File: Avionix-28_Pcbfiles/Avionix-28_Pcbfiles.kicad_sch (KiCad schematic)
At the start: 13 parts, among them J1 Conn_01x02_Pin, J2 Conn_01x02_Pin, U1 TPS54202DDCR

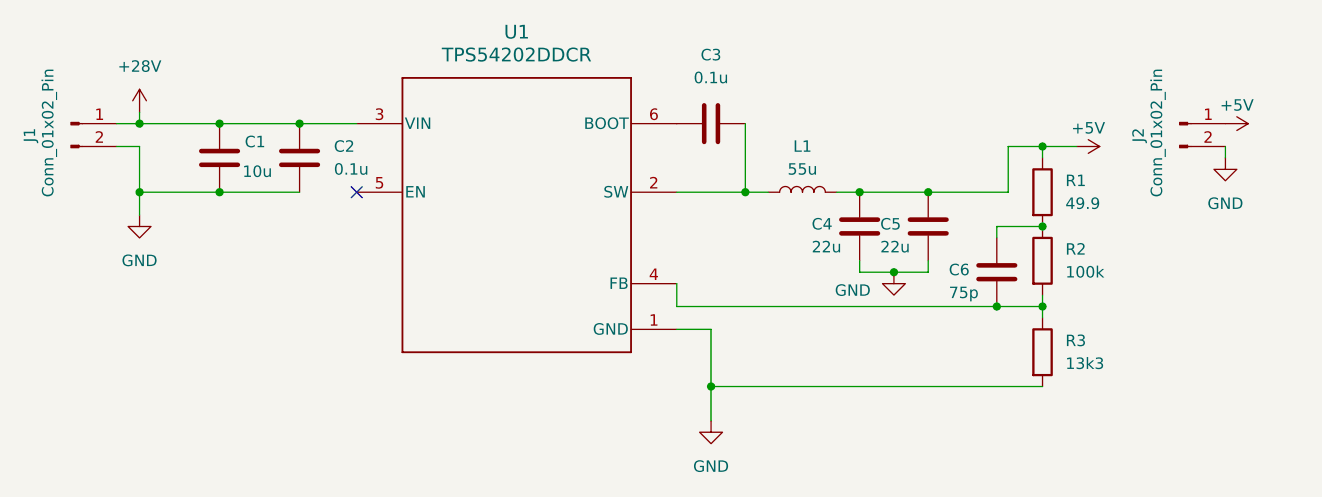
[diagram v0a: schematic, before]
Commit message: changed inductor value and assigned footprints
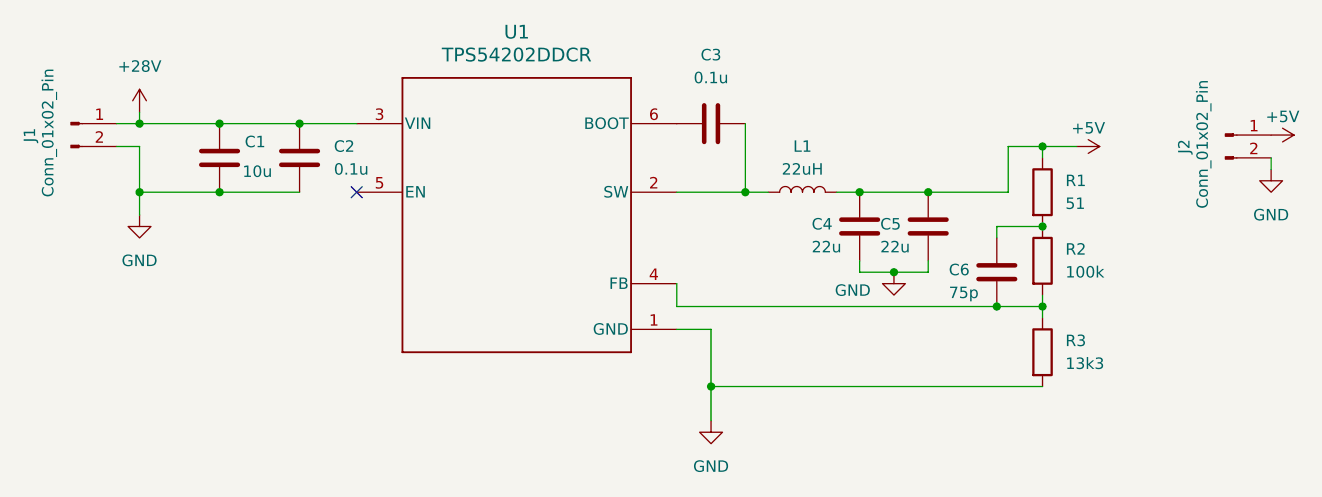
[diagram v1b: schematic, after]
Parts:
- C1, C4, C5: footprint (none) -> Capacitor_SMD:C_1210_3225Metric
- C2, C3: footprint (none) -> Capacitor_SMD:C_0402_1005Metric
- C6: footprint (none) -> Capacitor_SMD:C_0805_2012Metric
- J1, J2: footprint Avionix_fprints:CUI_TB007-508-02BE -> Screw_terminal:Connector_PinHeader_3.81
- L1: value 55u -> 22uH
- R1: value 49.9 -> 51; footprint (none) -> Resistor_SMD:R_0805_2012Metric
- R2, R3: footprint (none) -> Resistor_SMD:R_0805_2012Metric
- U1: footprint DDC0006A_N -> Screw_terminal:DDC0006A_N
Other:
- moved on the sheet: J2
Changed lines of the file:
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@@
 	(wire
 		(pts
-			(xy 172.72 77.47) (xy 172.72 76.2)
+			(xy 177.8 78.74) (xy 177.8 77.47)
 		)
 		(stroke
@@
 			)
 		)
-		(property "Footprint" ""
+		(property "Footprint" "Resistor_SMD:R_0805_2012Metric"
 			(at 150.622 99.06 90)
 			(hide yes)
@@
 	(symbol
 		(lib_id "power:GND")
-		(at 172.72 77.47 0)
+		(at 177.8 78.74 0)
 		(unit 1)
 		(body_style 1)
@@
 		(fields_autoplaced yes)
 		(property "Reference" "#PWR04"
-			(at 172.72 83.82 0)
+			(at 177.8 85.09 0)
 			(hide yes)
 			(show_name no)
@@
 		)
 		(property "Value" "GND"
-			(at 172.72 82.55 0)
+			(at 177.8 83.82 0)
 			(show_name no)
 			(do_not_autoplace no)
@@
 		)
 		(property "Footprint" ""
-			(at 172.72 77.47 0)
-			(hide yes)
-			(show_name no)
-			(do_not_autoplace no)
-			(effects
-				(font
-					(size 1.27 1.27)
-				)
-			)
-		)
-		(property "Datasheet" ""
-			(at 172.72 77.47 0)
+			(at 177.8 78.74 0)
+			(hide yes)
+			(show_name no)
+			(do_not_autoplace no)
+			(effects
+				(font
+					(size 1.27 1.27)
+				)
+			)
+		)
+		(property "Datasheet" ""
+			(at 177.8 78.74 0)
 			(hide yes)
 			(show_name no)
@@
 		)
 		(property "Description" "Power symbol creates a global label with name \"GND\" , ground"
-			(at 172.72 77.47 0)
+			(at 177.8 78.74 0)
 			(hide yes)
 			(show_name no)
@@
 			)
 		)
-		(property "Footprint" "DDC0006A_N"
+		(property "Footprint" "Screw_terminal:DDC0006A_N"
 			(at 93.98 83.82 0)
 			(hide yes)
@@
 			)
 		)
-		(property "Footprint" ""
+		(property "Footprint" "Capacitor_SMD:C_0805_2012Metric"
 			(at 146.3548 86.36 0)
 			(hide yes)
@@
 			)
 		)
-		(property "Footprint" ""
+		(property "Footprint" "Capacitor_SMD:C_0402_1005Metric"
 			(at 119.38 72.6948 0)
 			(hide yes)
@@
 			)
 		)
-		(property "Footprint" ""
+		(property "Footprint" "Capacitor_SMD:C_1210_3225Metric"
 			(at 138.7348 81.28 0)
 			(hide yes)
@@
 	(symbol
 		(lib_id "power:+5V")
-		(at 172.72 73.66 270)
+		(at 177.8 74.93 270)
 		(unit 1)
 		(body_style 1)
@@
 		(dnp no)
 		(property "Reference" "#PWR05"
-			(at 168.91 73.66 0)
+			(at 173.99 74.93 0)
 			(hide yes)
 			(show_name no)
@@
 		)
 		(property "Value" "+5V"
-			(at 173.99 71.628 90)
+			(at 179.07 72.898 90)
 			(show_name no)
 			(do_not_autoplace no)
@@
 		)
 		(property "Footprint" ""
-			(at 172.72 73.66 0)
-			(hide yes)
-			(show_name no)
-			(do_not_autoplace no)
-			(effects
-				(font
-					(size 1.27 1.27)
-				)
-			)
-		)
-		(property "Datasheet" ""
-			(at 172.72 73.66 0)
+			(at 177.8 74.93 0)
+			(hide yes)
+			(show_name no)
+			(do_not_autoplace no)
+			(effects
+				(font
+					(size 1.27 1.27)
+				)
+			)
+		)
+		(property "Datasheet" ""
+			(at 177.8 74.93 0)
 			(hide yes)
 			(show_name no)
@@
 		)
 		(property "Description" "Power symbol creates a global label with name \"+5V\""
-			(at 172.72 73.66 0)
+			(at 177.8 74.93 0)
 			(hide yes)
 			(show_name no)
@@
 			)
 		)
-		(property "Footprint" ""
+		(property "Footprint" "Resistor_SMD:R_0805_2012Metric"
 			(at 150.622 88.9 90)
 			(hide yes)
@@
 			)
 		)
-		(property "Footprint" "Avionix_fprints:CUI_TB007-508-02BE"
+		(property "Footprint" "Screw_terminal:Connector_PinHeader_3.81"
 			(at 44.45 73.66 0)
 			(hide yes)
@@
 	(symbol
 		(lib_id "Connector:Conn_01x02_Pin")
-		(at 167.64 73.66 0)
+		(at 172.72 74.93 0)
 		(unit 1)
 		(body_style 1)
@@
 		(dnp no)
 		(property "Reference" "J2"
-			(at 163.068 74.93 90)
+			(at 168.148 76.2 90)
 			(show_name no)
 			(do_not_autoplace no)
@@
 		)
 		(property "Value" "Conn_01x02_Pin"
-			(at 165.1 74.676 90)
-			(show_name no)
-			(do_not_autoplace no)
-			(effects
-				(font
-					(size 1.27 1.27)
-				)
-			)
-		)
-		(property "Footprint" "Avionix_fprints:CUI_TB007-508-02BE"
-			(at 167.64 73.66 0)
-			(hide yes)
-			(show_name no)
-			(do_not_autoplace no)
-			(effects
-				(font
-					(size 1.27 1.27)
-				)
-			)
-		)
-		(property "Datasheet" ""
-			(at 167.64 73.66 0)
+			(at 170.18 75.946 90)
+			(show_name no)
+			(do_not_autoplace no)
+			(effects
+				(font
+					(size 1.27 1.27)
+				)
+			)
+		)
+		(property "Footprint" "Screw_terminal:Connector_PinHeader_3.81"
+			(at 172.72 74.93 0)
+			(hide yes)
+			(show_name no)
+			(do_not_autoplace no)
+			(effects
+				(font
+					(size 1.27 1.27)
+				)
+			)
+		)
+		(property "Datasheet" ""
+			(at 172.72 74.93 0)
 			(hide yes)
 			(show_name no)
@@
 		)
 		(property "Description" "Generic connector, single row, 01x02, script generated"
-			(at 167.64 73.66 0)
+			(at 172.72 74.93 0)
 			(hide yes)
 			(show_name no)
@@
 			)
 		)
-		(property "Footprint" ""
+		(property "Footprint" "Capacitor_SMD:C_1210_3225Metric"
 			(at 131.1148 81.28 0)
 			(hide yes)
@@
 			)
 		)
-		(property "Footprint" ""
+		(property "Footprint" "Capacitor_SMD:C_1210_3225Metric"
 			(at 61.9252 81.28 0)
 			(hide yes)
@@
 			)
 		)
-		(property "Footprint" ""
+		(property "Footprint" "Capacitor_SMD:C_0402_1005Metric"
 			(at 70.8152 81.28 0)
 			(hide yes)
@@
 			)
 		)
-		(property "Value" "49.9"
+		(property "Value" "51"
 			(at 154.94 82.5499 0)
 			(show_name no)
@@
 			)
 		)
-		(property "Footprint" ""
+		(property "Footprint" "Resistor_SMD:R_0805_2012Metric"
 			(at 150.622 81.28 90)
 			(hide yes)
@@
 			)
 		)
-		(property "Value" "55u"
+		(property "Value" "22uH"
 			(at 125.73 78.74 90)
 			(show_name no)

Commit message: -
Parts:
- L1: footprint (none) -> Screw_terminal:IND_CD54_SUM
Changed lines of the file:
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@@
 			)
 		)
-		(property "Footprint" ""
+		(property "Footprint" "Screw_terminal:IND_CD54_SUM"
 			(at 125.73 81.28 0)
 			(hide yes)
